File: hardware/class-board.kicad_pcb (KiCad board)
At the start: 4 copper layers, 180 x 100 mm, 405 parts, among them J1 DevKit J1 (left row), J2 DevKit J3 (right row), J201 USB-C 16P, J202 DC005-T20, J3 Qwiic, J4 Qwiic, J401 KF301-5.0-3P, J402 KF301-5.0-3P, J403 KF301-5.0-3P, J404 KF301-5.0-3P, J411 KF301-5.0-2P, J412 KF301-5.0-2P, J5 Expansion 2x10, J501 KF301-5.0-2P, J502 KF301-5.0-2P, J503 KF301-5.0-2P, J504 KF301-5.0-2P, J505 KF301-5.0-2P, J506 KF301-5.0-2P, J507 KF301-5.0-2P, J6 Panel link 2x20 R/A, J802 KF301-5.0-2P, J901 KF301-5.0-2P, J903 KF301-5.0-2P, J905 KF301-5.0-3P, K401 HK4100F-DC5V-SHG, K402 HK4100F-DC5V-SHG, K403 HK4100F-DC5V-SHG, K404 HK4100F-DC5V-SHG, Q401 AO3400A, Q402 AO3400A, Q403 AO3400A, Q404 AO3400A, Q411 MMBT5551, Q412 MMBT5551, Q421 MMBT5551, Q422 MMBT5551, Q901 AOD4185, Q904 AOD4184A, U101 ADS8688IDBTR, U201 LM66100DCKR, U202 LM66100DCKR, U203 78L05G-AB3-R, U204 AMS1117-3.3, U301 DAC8563SDGSR, U302 74HCT125PW, U303 OPA2192IDR, U401 6N137S-TA1-L, U402 6N137S-TA1-L, U501 SN74AHCT541PWR, U502 74HCT125PW, U503 SN74LVC1T45DBVR, U504 SN74LVC1G17DBVR, U505 TCA9535PWR, U701 SI5351A-B-GT, U702 74HC74D,653, U703 OPA1656IDR, U704 DG419DY-T1-E3, U705 OPA1612AIDR, U706 OPA1612AIDR, U801 AD9834BRUZ, U802 OPA564AIDWPR, U901 TS5A23157DGSR, U902 TS5A23157DGSR, U903 DRV8871DDAR, U904 UCC27517DBVR, X501 10 MHz TCXO, Y701 25 MHz

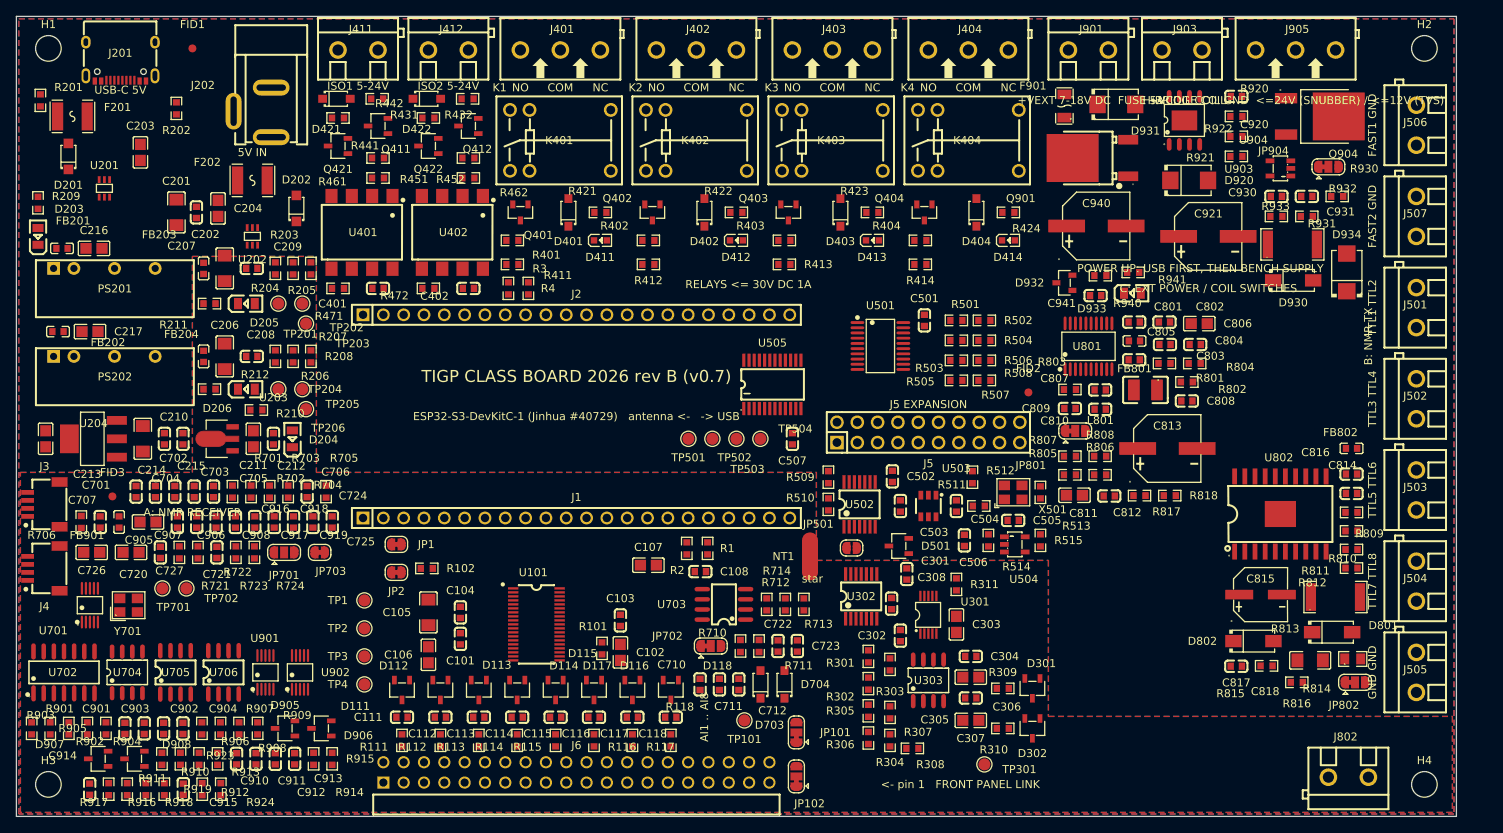
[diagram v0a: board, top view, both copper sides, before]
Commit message: hardware: main-board PCB regenerated to the v0.7b schematic (Decision #55): three bottom-side link headers, 10 A relay row with terminals behind it, rear-edge connectors take wires from the edge, MAINS spacing; DRC 0 errors, 499 unrouted (no routing yet); renders + zone map; 2026-09-13 PCB kept in release/pre-rework-20260913 on the master
Co-Authored-By: Claude Fable 5.1 <noreply@anthropic.com>
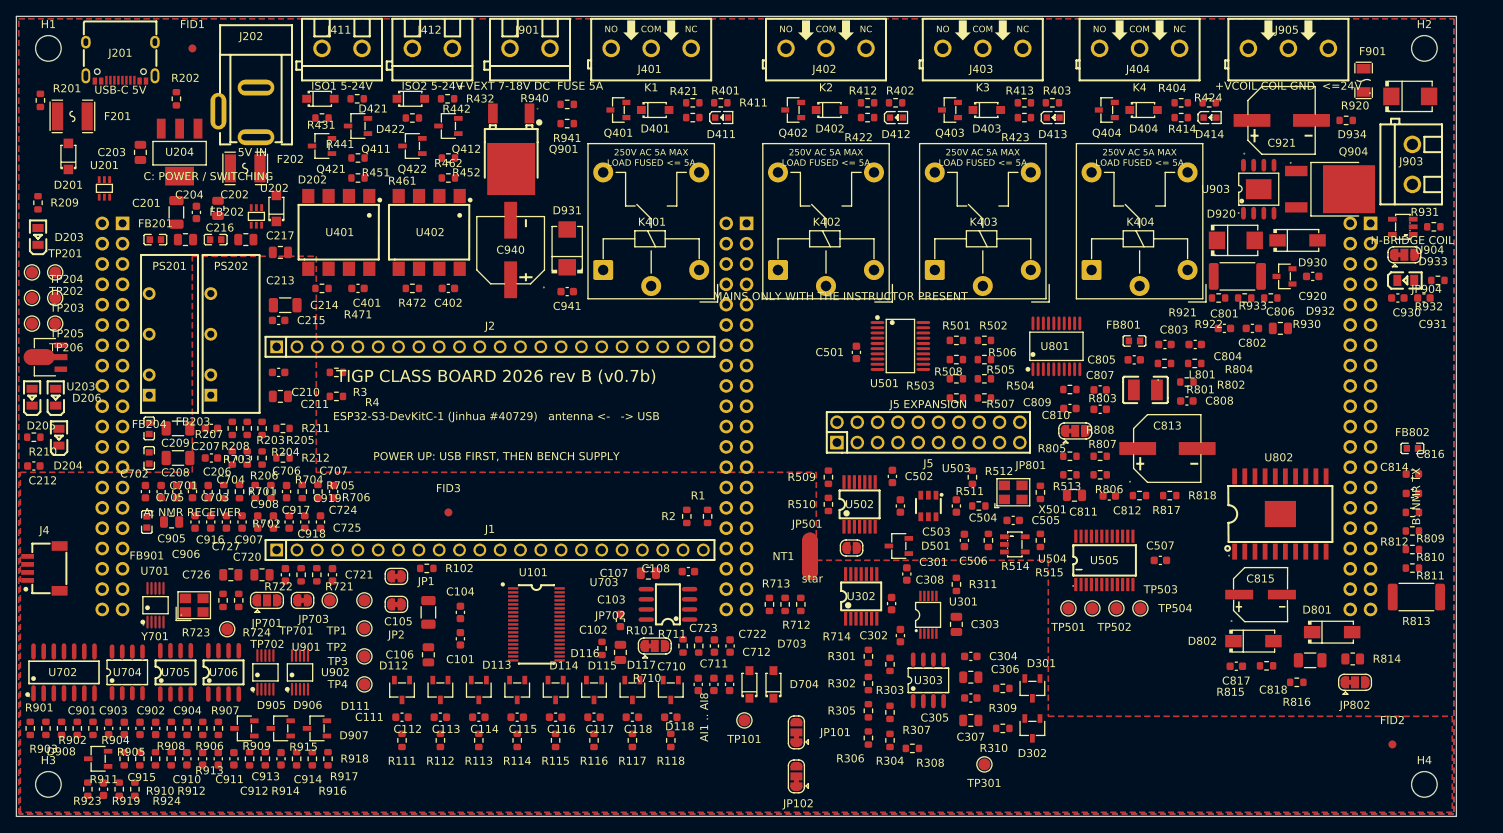
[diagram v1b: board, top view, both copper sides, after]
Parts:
- removed J3: Qwiic, class_board:CONN-SMD_4P-P1.00_XY-SM04B-SRSS-TB
- removed J501, J502, J503, J504, J505, J506, J507, J802: KF301-5.0-2P, class_board:CONN-TH_P5.00_KF301-5.0-2P
- added J7: Panel link 2x20 male, Connector_PinHeader_2.54mm:PinHeader_2x20_P2.54mm_Vertical, B.Cu at (91.3, 25.9)
- added J8: Panel link 2x20 male, Connector_PinHeader_2.54mm:PinHeader_2x20_P2.54mm_Vertical, B.Cu at (169.3, 25.9)
- C101, C103, C104, C108, C111, C112, C113, C114, C115, C116, C117, C118, C202, C208, C209, C210, C212, C215, C301, C302, C304, C305, C308, C401, C402, C501, C502, C503, C504, C505, C506, C507, C701, C702, C703, C704, C705, C706, C707, C710, C711, C712, C720, C721, C722, C723, C724, C725, C801, C802, C803, C804, C805, C807, C808, C809, C810, C812, C814, C816, C817, C901, C902, C903, C904, C906, C907, C908, C910, C911, C912, C913, C914, C915, C916, C917, C918, C919, C920, C930, C931, C941: footprint class_board:C0603 -> Capacitor_SMD:C_0603_1608Metric
- C102, C106, C107, C203, C204, C211, C213, C216, C217, C303, C306, C307, C726, C727, C806, C811, C905: footprint class_board:C0805 -> Capacitor_SMD:C_0805_2012Metric
- C105, C201, C206, C207, C214, C818: footprint class_board:C1206 -> Capacitor_SMD:C_1206_3216Metric
- J6: value Panel link 2x20 R/A -> Panel link 2x20 male; footprint class_board:HDR-TH_40P-P2.54-H-R2-C20-S2.54-W10.0 -> Connector_PinHeader_2.54mm:PinHeader_2x20_P2.54mm_Vertical; moved to B.Cu
- K401, K402, K403, K404: value HK4100F-DC5V-SHG -> JQC-3FF/005-1ZS; footprint class_board:RELAY-TH_HK4100F-DC5V-SHG -> Relay_THT:Relay_SPDT_Hongfa_JQC-3FF_0XX-1Z
- R1, R101, R102, R111, R112, R113, R114, R115, R116, R117, R118, R2, R201, R202, R203, R204, R205, R206, R207, R208, R209, R210, R211, R212, R3, R301, R302, R303, R304, R305, R306, R307, R308, R309, R310, R311, R4, R401, R402, R403, R404, R411, R412, R413, R414, R421, R422, R423, R424, R431, R432, R441, R442, R451, R452, R461, R462, R471, R472, R501, R502, R503, R504, R505, R506, R507, R508, R509, R510, R511, R512, R513, R514, R515, R701, R702, R703, R704, R705, R706, R710, R711, R712, R713, R714, R721, R722, R723, R724, R801, R802, R803, R804, R805, R806, R807, R808, R809, R810, R811, R812, R815, R816, R817, R818, R901, R902, R903, R904, R905, R906, R907, R908, R909, R910, R911, R912, R913, R914, R915, R916, R917, R918, R919, R920, R921, R922, R923, R924, R930, R931, R932, R940, R941: footprint class_board:R0603 -> Resistor_SMD:R_0603_1608Metric
- R813, R933: footprint class_board:R2512 -> Resistor_SMD:R_2512_6332Metric
- R814: footprint class_board:R0805 -> Resistor_SMD:R_0805_2012Metric
- moved J6 89.0 mm to (13.3, 25.9), turned to 180 degrees
- moved Q901 73.7 mm to (61.9, 15.6), turned to 90 degrees
- moved C940 73.3 mm to (61.8, 29.2), turned to 90 degrees
- moved R941 73.2 mm to (68.8, 13.4)
- moved D931 71.0 mm to (68.8, 29.0), turned to 90 degrees
- moved R940 70.0 mm to (68.8, 11.0)
- moved J901 69.8 mm to (64.2, 4.00), turned to 180 degrees
- moved C941 66.1 mm to (68.8, 34.4)
- moved FID2 63.3 mm to (172.0, 91.0)
- moved TP501 52.0 mm to (131.5, 74.0)
- moved TP502 52.0 mm to (134.5, 74.0)
- moved TP503 52.0 mm to (137.5, 74.0)
- moved TP504 52.0 mm to (140.5, 74.0)
- moved C507 48.4 mm to (143.0, 68.0), turned to 0 degrees
- moved U505 47.0 mm to (136.0, 68.0)
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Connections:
- J6 pad 1: AO1 -> AI1
- J6 pad 11: AI2 -> AI6
- J6 pad 13: AI3 -> AI7
- J6 pad 15: AI4 -> AI8
- J6 pad 17: AI5 -> RX
- J6 pad 19: AI6 -> TX
- J6 pad 21: AI7 -> TX
- J6 pad 23: AI8 -> AUX
- J6 pad 25: I2C_SDA -> AO1
- J6 pad 26: GND -> AGND
- J6 pad 27: I2C_SCL -> AO2
- J6 pad 28: GND -> AGND
- J6 pad 29: +3V3 -> unconnected-(J6-Pad29)
- J6 pad 3: AO2 -> AI2
- J6 pad 30: GND -> AGND
- J6 pad 31: +3V3 -> unconnected-(J6-Pad31)
- J6 pad 32: GND -> AGND
- J6 pad 33: LED_WIFI -> unconnected-(J6-Pad33)
- J6 pad 34: GND -> AGND
- J6 pad 35: LED_ACT -> unconnected-(J6-Pad35)
- J6 pad 36: GND -> AGND
- J6 pad 37: RX -> unconnected-(J6-Pad37)
- J6 pad 39: TX -> unconnected-(J6-Pad39)
- J6 pad 5: TRIG_5V -> AI3
- J6 pad 6: GND -> AGND
- J6 pad 7: AUX -> AI4
- J6 pad 9: AI1 -> AI5
- R501 pad 2: /b5_dio_trig/TTL1 -> TTL1
- R502 pad 2: /b5_dio_trig/TTL2 -> TTL2
- R503 pad 2: /b5_dio_trig/TTL3 -> TTL3
- R504 pad 2: /b5_dio_trig/TTL4 -> TTL4
- R505 pad 2: /b5_dio_trig/TTL5 -> TTL5
- R506 pad 2: /b5_dio_trig/TTL6 -> TTL6
- R507 pad 2: /b5_dio_trig/TTL7 -> TTL7
- R508 pad 2: /b5_dio_trig/TTL8 -> TTL8
- R509 pad 2: /b5_dio_trig/FASTTTL1 -> FASTTTL1
- R510 pad 2: /b5_dio_trig/FASTTTL2 -> FASTTTL2
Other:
- board text added: "+VCOIL COIL GND <=24V"
- board text added: "250V AC 5A MAX"
- board text added: "C: POWER / SWITCHING"
- board text added: "J6 PANEL LINK pin 1 ->"
- board text added: "J7 PANEL LINK pin 1 ->"
- board text added: "J8 PANEL LINK pin 1 ->"
- board text added: "LOAD FUSED <= 5A"
- board text added: "MAINS ONLY WITH THE INSTRUCTOR PRESENT"
- board text added: "TIGP CLASS BOARD 2026 rev B (v0.7b)"
- board text removed: "+VCOIL COIL GND <=24V (SNUBBER) / <=12V (TVS)"
- board text removed: "<- pin 1 FRONT PANEL LINK"
- board text removed: "C: EXT POWER / COIL SWITCHES"
- board text removed: "FAST1 GND"
- board text removed: "FAST2 GND"
- board text removed: "GND GND"
- board text removed: "RELAYS <= 30V DC 1A"
- board text removed: "TIGP CLASS BOARD 2026 rev B (v0.7)"
- board text removed: "TTL1 TTL2"
- board text removed: "TTL3 TTL4"
- board text removed: "TTL5 TTL6"
- board text removed: "TTL7 TTL8"

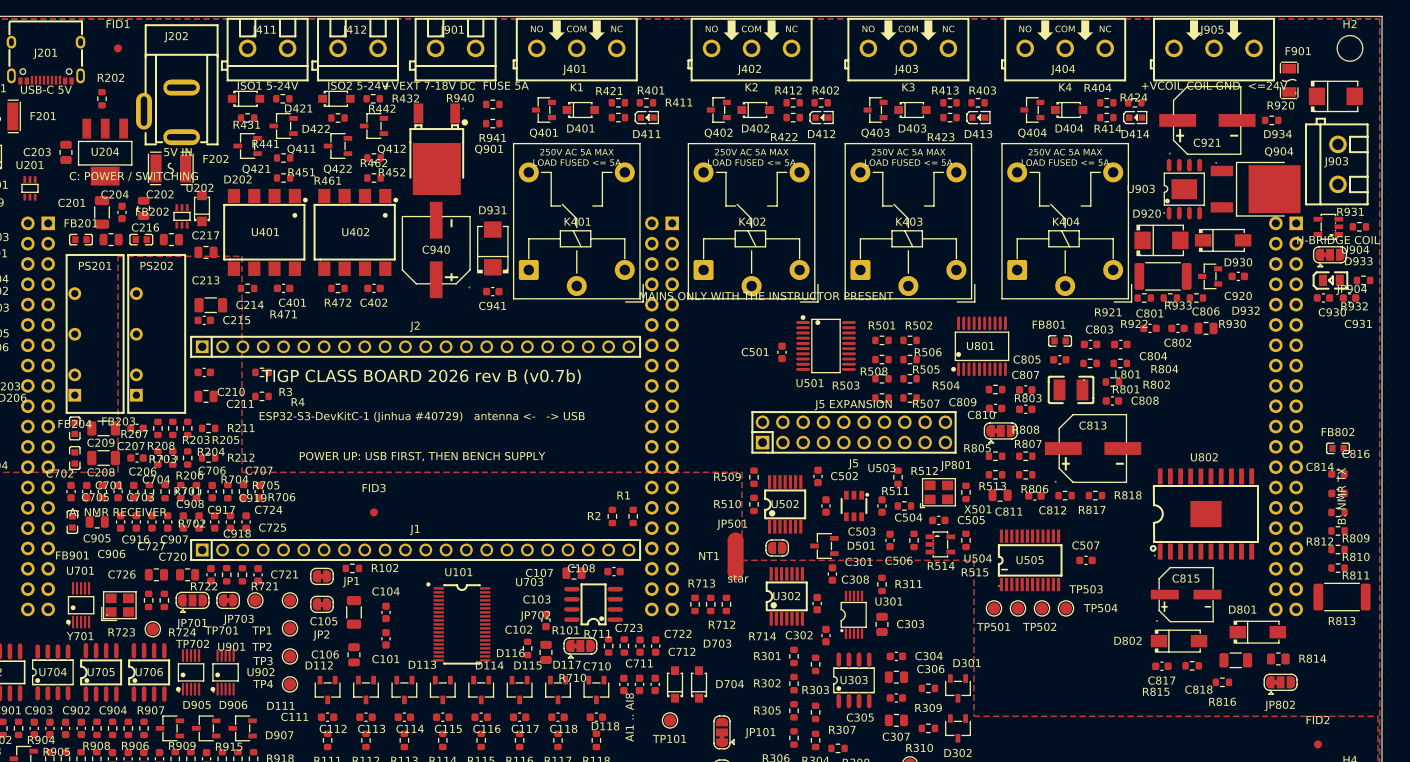
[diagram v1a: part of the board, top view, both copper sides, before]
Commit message: v0.7d: relays and mains removed, MODULE OUT 1-7 (5 V TTL) on a shrouded 2x6 header on the front panel, isolated inputs moved to the panel, section C = the front-panel board (4-layer, 18 mm SMA grid, OLED clear of headers, unrouted student copy), main board re-placed; workbook, tutor guide, firmware docs, hardware docs updated (Decision #58)
Co-Authored-By: Claude Fable 5.1 <noreply@anthropic.com>
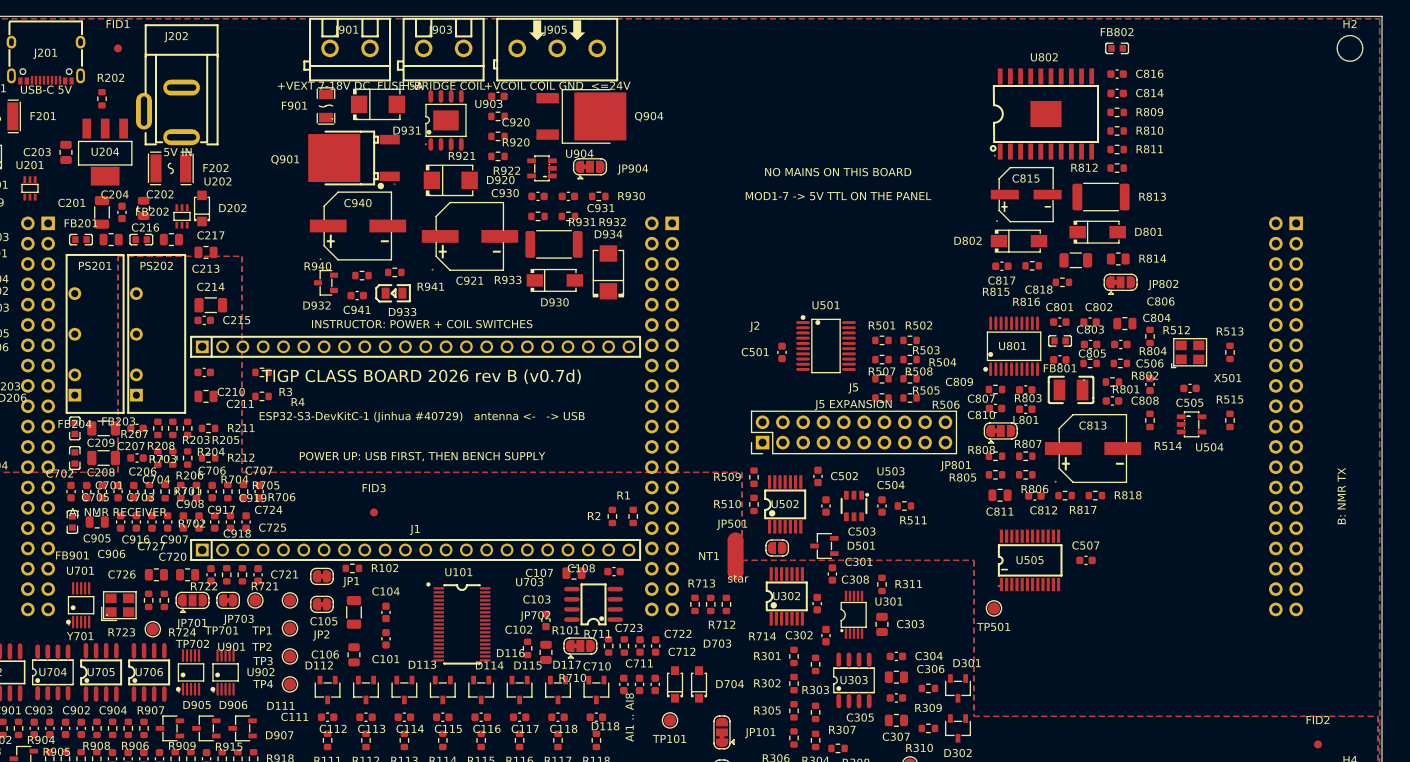
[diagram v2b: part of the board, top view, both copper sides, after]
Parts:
- removed C401, C402: 100nF, Capacitor_SMD:C_0603_1608Metric
- removed D401, D402, D403, D404, D421, D422: 1N4148W, class_board:SOD-123F_L2.7-W1.6-LS3.8-RD
- removed D411, D412, D413, D414: YELLOW, class_board:LED0603-RD-YELLOW
- removed J401, J402, J403, J404: KF301-5.0-3P, class_board:CONN-TH_3P-P5.00_KF301-5.0-3P
- removed J411, J412: KF301-5.0-2P, class_board:CONN-TH_P5.00_KF301-5.0-2P
- removed K401, K402, K403, K404: JQC-3FF/005-1ZS, Relay_THT:Relay_SPDT_Hongfa_JQC-3FF_0XX-1Z
- removed Q401, Q402, Q403, Q404: AO3400A, class_board:SOT-23-3_L2.9-W1.3-P1.90-LS2.4-BR
- removed Q411, Q412, Q421, Q422: MMBT5551, class_board:SOT-23-3_L2.9-W1.6-P1.90-LS2.8-BR
- removed R401, R402, R403, R404, R461, R462, R471, R472: 1k, Resistor_SMD:R_0603_1608Metric
- removed R411, R412, R413, R414, R441, R442: 10k, Resistor_SMD:R_0603_1608Metric
- removed R421, R422, R423, R424: 2.2k, Resistor_SMD:R_0603_1608Metric
- removed R431, R432: 220, Resistor_SMD:R_0603_1608Metric
- removed R451, R452: 100, Resistor_SMD:R_0603_1608Metric
- removed TP502, TP503, TP504: TP, class_board:TestPoint_Pad_D1.5mm
- removed U401, U402: 6N137S-TA1-L, class_board:SOP-8_L9.8-W6.6-P2.54-LS10.3-BL
- J5: footprint class_board:HDR-TH_20P-P2.54-V-M-R2-C10-S2.54 -> Connector_PinHeader_2.54mm:PinHeader_2x10_P2.54mm_Vertical
- moved F901 120.4 mm to (48.0, 11.2)
- moved D933 117.2 mm to (56.5, 34.6)
- moved J903 112.7 mm to (62.7, 4.00), turned to 180 degrees
- moved D932 110.5 mm to (48.0, 33.3)
- moved R931 102.7 mm to (74.5, 25.0)
- moved R932 99.7 mm to (78.3, 25.0)
- moved C930 99.0 mm to (74.5, 22.5)
- moved U904 98.6 mm to (75.0, 19.0)
- moved C931 98.5 mm to (78.3, 22.5)
- moved R920 96.7 mm to (69.5, 12.5)
- moved C920 95.2 mm to (69.5, 10.0)
- moved D934 93.6 mm to (83.3, 32.0), turned to 90 degrees
- moved C921 93.3 mm to (66.0, 27.5)
- moved JP904 93.2 mm to (81.0, 18.8)
- moved U903 92.7 mm to (63.0, 13.0)
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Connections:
- J8 pad 19: unconnected-(J8-Pad19) -> MOD1
- J8 pad 21: unconnected-(J8-Pad21) -> MOD2
- J8 pad 23: unconnected-(J8-Pad23) -> MOD3
- J8 pad 25: unconnected-(J8-Pad25) -> MOD4
- J8 pad 27: unconnected-(J8-Pad27) -> MOD5
- J8 pad 29: unconnected-(J8-Pad29) -> MOD6
- J8 pad 31: unconnected-(J8-Pad31) -> MOD7
- J8 pad 35: unconnected-(J8-Pad35) -> OPTO_IN1
- J8 pad 37: unconnected-(J8-Pad37) -> OPTO_IN2
- U505 pad 13: RLY_IN1 -> MOD1
- U505 pad 14: RLY_IN2 -> MOD2
- U505 pad 15: RLY_IN3 -> MOD3
- U505 pad 16: RLY_IN4 -> MOD4
- U505 pad 18: EXP_P15 -> MOD5
- U505 pad 19: EXP_P16 -> MOD6
- U505 pad 20: EXP_P17 -> MOD7
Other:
- board text added: "INSTRUCTOR: POWER + COIL SWITCHES"
- board text added: "MOD1-7 -> 5V TTL ON THE PANEL"
- board text added: "NO MAINS ON THIS BOARD"
- board text added: "TIGP CLASS BOARD 2026 rev B (v0.7d)"
- board text removed: "250V AC 5A MAX"
- board text removed: "C: POWER / SWITCHING"
- board text removed: "COM"
- board text removed: "ISO1 5-24V"
- board text removed: "ISO2 5-24V"
- board text removed: "K1"
- board text removed: "K2"
- board text removed: "K3"
- board text removed: "K4"
- board text removed: "LOAD FUSED <= 5A"
- board text removed: "MAINS ONLY WITH THE INSTRUCTOR PRESENT"
- board text removed: "NC"
- board text removed: "NO"
- board text removed: "TIGP CLASS BOARD 2026 rev B (v0.7b)"

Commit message: main board: link sockets J6/J7/J8 are female (PinSocket_2x20) on the bottom side, panel headers male (Decision #62); placement regenerated after the density pass, DRC 0 errors, unrouted; schematic + netlist + scripts
Co-Authored-By: Claude Fable 5.1 <noreply@anthropic.com>
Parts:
- J6, J7, J8: value Panel link 2x20 male -> Panel link 2x20 female; footprint Connector_PinHeader_2.54mm:PinHeader_2x20_P2.54mm_Vertical -> Connector_PinSocket_2.54mm:PinSocket_2x20_P2.54mm_Vertical
- moved TP4 59.1 mm to (98.3, 61.5)
- moved TP2 57.7 mm to (98.3, 58.5)
- moved TP3 54.7 mm to (95.0, 61.5)
- moved TP1 53.5 mm to (95.0, 58.5)
- moved U505 50.5 mm to (108.0, 26.0)
- moved C507 49.9 mm to (116.0, 26.0)
- moved TP501 49.1 mm to (121.0, 26.0)
- moved JP1 48.0 mm to (95.5, 69.0)
- moved JP2 48.0 mm to (95.5, 72.5)
- moved R501 32.5 mm to (116.0, 8.00)
- moved R502 32.5 mm to (119.5, 8.00)
- moved R503 32.5 mm to (116.0, 10.4)
- moved R504 32.5 mm to (119.5, 10.4)
- moved R505 32.5 mm to (116.0, 12.8)
- moved R506 32.5 mm to (119.5, 12.8)
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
